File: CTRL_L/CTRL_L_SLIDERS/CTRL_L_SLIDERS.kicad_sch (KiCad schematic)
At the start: 1 part, among them J1 Conn_01x04_Socket

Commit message: Finished Volume/Brightness Slider Daugherboard!
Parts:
- removed J1: Conn_01x04_Socket, symbol Connector:Conn_01x04_Socket
- added J1: BM04B-NSHSS-TBT_LF__SN_, BM04BNSHSSTBTLFSN, symbol BM04B-NSHSS-TBT_LF__SN_:BM04B-NSHSS-TBT_LF__SN_
- added VR1, VR2: RA2043F-20-10EB1-B10K, RA2043F2010EB1B10K, symbol RA2043F-20-10EB1-B10K:RA2043F-20-10EB1-B10K
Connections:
- new net +3V3: J1.4, VR1.3, VR2.3
- new net GND: J1.1, J1.5 (MP1), J1.6 (MP2), VR1.1, VR2.1
- new net SL_BRI: J1.2, VR2.2
- new net SL_VOL: J1.3, VR1.2

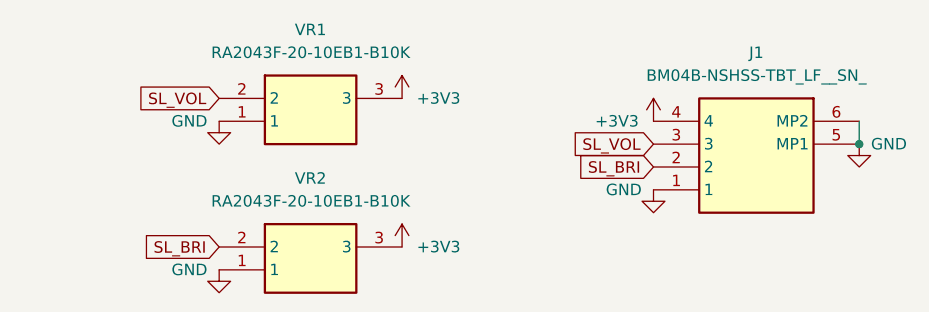
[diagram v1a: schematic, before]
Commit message: Removed the test points because i dont know what im doing.
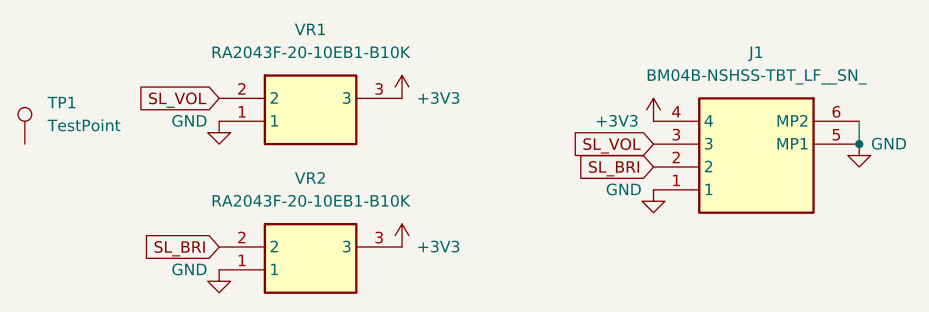
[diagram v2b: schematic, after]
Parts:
- added TP1: TestPoint, TestPoint:TestPoint_Keystone_5000-5004_Miniature, symbol Connector:TestPoint
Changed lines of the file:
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@@
+	)
+	(symbol
+		(lib_id "Connector:TestPoint")
+		(at 109.22 104.14 0)
+		(unit 1)
+		(body_style 1)
+		(exclude_from_sim no)
+		(in_bom yes)
+		(on_board yes)
+		(in_pos_files yes)
+		(dnp no)
+		(fields_autoplaced yes)
+		(property "Reference" "TP1"
+			(at 111.76 99.5679 0)
+			(show_name no)
+			(do_not_autoplace no)
+			(effects
+				(font
+					(size 1.27 1.27)
+				)
+				(justify left)
+			)
+		)
+		(property "Value" "TestPoint"
+			(at 111.76 102.1079 0)
+			(show_name no)
+			(do_not_autoplace no)
+			(effects
+				(font
+					(size 1.27 1.27)
+				)
+				(justify left)
+			)
+		)
+		(property "Footprint" "TestPoint:TestPoint_Keystone_5000-5004_Miniature"
+			(at 114.3 104.14 0)
+			(hide yes)
+			(show_name no)
+			(do_not_autoplace no)
+			(effects
+				(font
+					(size 1.27 1.27)
+				)
+			)
+		)
+		(property "Datasheet" ""
+			(at 114.3 104.14 0)
+			(hide yes)
+			(show_name no)
+			(do_not_autoplace no)
+			(effects
+				(font
+					(size 1.27 1.27)
+				)
+			)
+		)
+		(property "Description" "test point"
+			(at 109.22 104.14 0)
+			(hide yes)
+			(show_name no)
+			(do_not_autoplace no)
+			(effects
+				(font
+					(size 1.27 1.27)
+				)
+			)
+		)
+		(pin "1"
+		)
+		(instances
+			(project "CTRL_L_SLIDERS"
+				(path "/0024df83-b57f-4d3c-8413-e5efc583cbbc"
+					(reference "TP1")
+					(unit 1)
+				)
+			)
+		)
 	)
 	(symbol

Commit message: Add LattePandaMu Board files, many fixes to do!
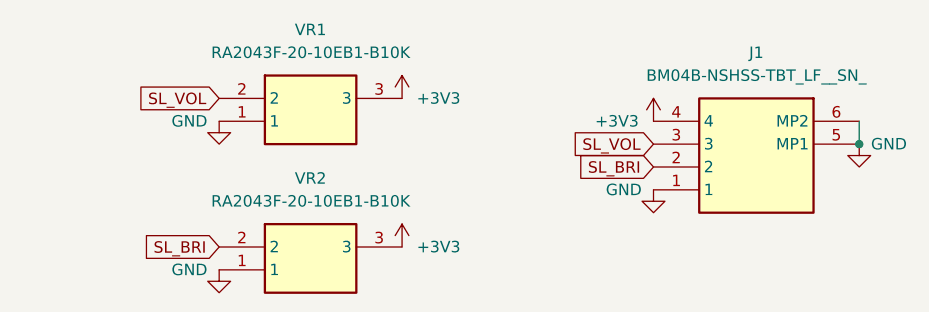
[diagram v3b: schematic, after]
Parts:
- removed TP1: TestPoint, TestPoint:TestPoint_Keystone_5000-5004_Miniature, symbol Connector:TestPoint
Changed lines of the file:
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@@
-	)
-	(symbol
-		(lib_id "Connector:TestPoint")
-		(at 109.22 104.14 0)
-		(unit 1)
-		(body_style 1)
-		(exclude_from_sim no)
-		(in_bom yes)
-		(on_board yes)
-		(in_pos_files yes)
-		(dnp no)
-		(fields_autoplaced yes)
-		(property "Reference" "TP1"
-			(at 111.76 99.5679 0)
-			(show_name no)
-			(do_not_autoplace no)
-			(effects
-				(font
-					(size 1.27 1.27)
-				)
-				(justify left)
-			)
-		)
-		(property "Value" "TestPoint"
-			(at 111.76 102.1079 0)
-			(show_name no)
-			(do_not_autoplace no)
-			(effects
-				(font
-					(size 1.27 1.27)
-				)
-				(justify left)
-			)
-		)
-		(property "Footprint" "TestPoint:TestPoint_Keystone_5000-5004_Miniature"
-			(at 114.3 104.14 0)
-			(hide yes)
-			(show_name no)
-			(do_not_autoplace no)
-			(effects
-				(font
-					(size 1.27 1.27)
-				)
-			)
-		)
-		(property "Datasheet" ""
-			(at 114.3 104.14 0)
-			(hide yes)
-			(show_name no)
-			(do_not_autoplace no)
-			(effects
-				(font
-					(size 1.27 1.27)
-				)
-			)
-		)
-		(property "Description" "test point"
-			(at 109.22 104.14 0)
-			(hide yes)
-			(show_name no)
-			(do_not_autoplace no)
-			(effects
-				(font
-					(size 1.27 1.27)
-				)
-			)
-		)
-		(pin "1"
-		)
-		(instances
-			(project "CTRL_L_SLIDERS"
-				(path "/0024df83-b57f-4d3c-8413-e5efc583cbbc"
-					(reference "TP1")
-					(unit 1)
-				)
-			)
-		)
 	)
 	(symbol
